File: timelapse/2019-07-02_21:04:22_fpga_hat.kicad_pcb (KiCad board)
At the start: 4 copper layers, 65 x 56.5 mm, 90 parts, among them J1 2x20, J2 AudioJack3, J3 Conn_02x06_Top_Bottom, J4 Conn_02x06_Top_Bottom, J5 Conn_02x06_Top_Bottom, J6 Conn_01x02, SW1 PTS815, SW2 PTS815, SW3 PTS815, SW4 PTS815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

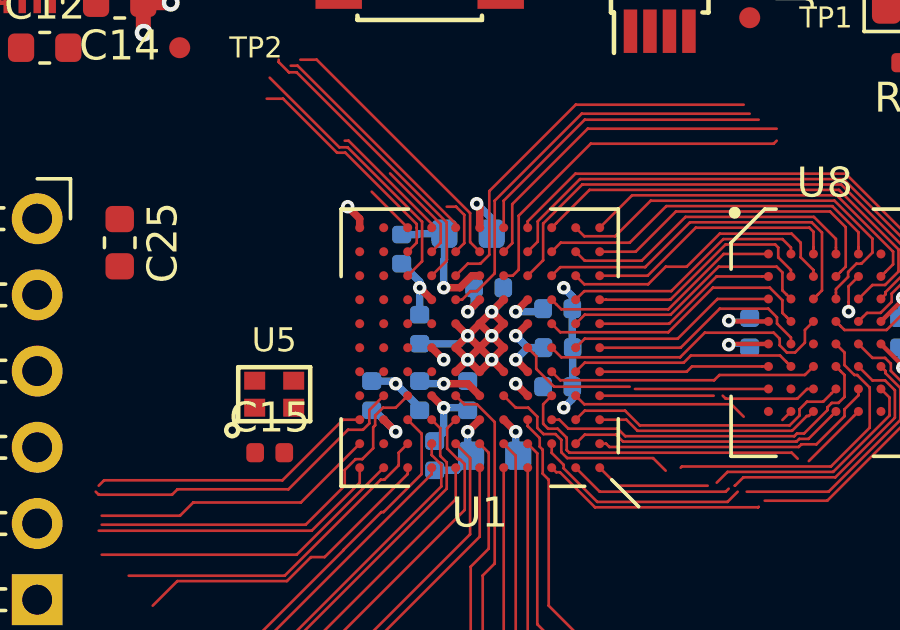
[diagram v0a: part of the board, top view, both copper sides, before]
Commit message: More FPGA escape
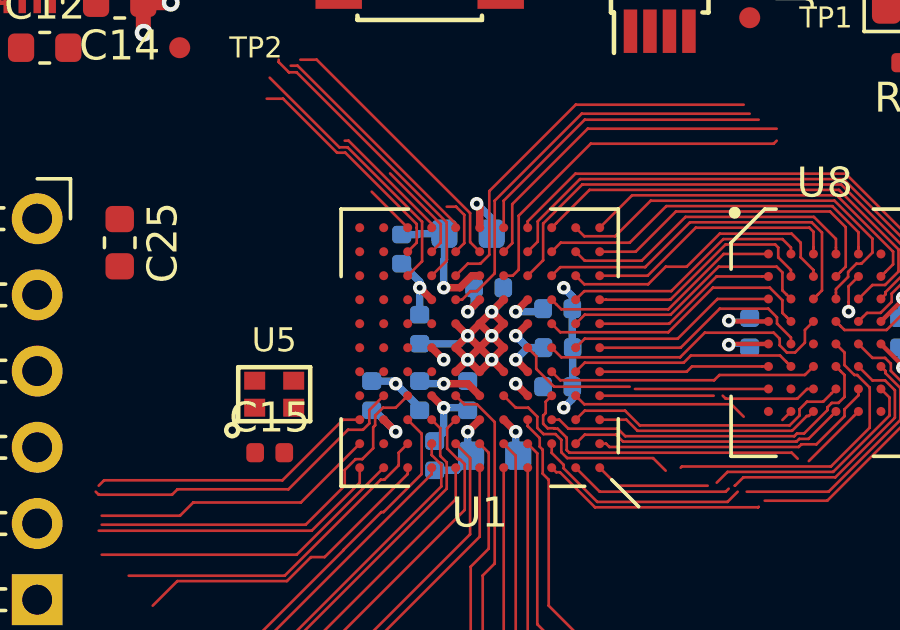
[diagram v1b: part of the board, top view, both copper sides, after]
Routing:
- net +3V3: track 13.9 -> 13.1 mm, vias 9 -> 8
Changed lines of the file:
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@@
     (thickness 1.6)
     (drawings 20)
-    (tracks 657)
+    (tracks 658)
     (zones 0)
     (modules 90)
@@
   )
   (setup
-    (last_trace_width 0.25)
+    (last_trace_width 0.09)
     (user_trace_width 0.15)
     (user_trace_width 0.25)
     (user_trace_width 0.5)
     (trace_clearance 0.09)
-    (zone_clearance 0.1)
+    (zone_clearance 0.2)
     (zone_45_only yes)
     (trace_min 0.09)
@@
   (segment (start 134.100004 106.5) (end 133.7 106.900004) (width 0.25) (layer B.Cu) (net 7))
   (segment (start 134.63 106.5) (end 134.100004 106.5) (width 0.25) (layer B.Cu) (net 7))
-  (via (at 128.1 101.8) (size 0.45) (drill 0.2) (layers F.Cu B.Cu) (net 7))
-  (segment (start 128.5 102.5) (end 128.5 102.2) (width 0.25) (layer F.Cu) (net 7))
-  (segment (start 128.5 102.2) (end 128.1 101.8) (width 0.25) (layer F.Cu) (net 7))
   (segment (start 116.5 95) (end 116.75 95) (width 0.15) (layer F.Cu) (net 9))
   (segment (start 115.5 94.485) (end 115.985 94.485) (width 0.15) (layer F.Cu) (net 9))
@@
   (segment (start 135.489099 110) (end 142.9 110) (width 0.09) (layer F.Cu) (net 118))
   (segment (start 135.4 109.910901) (end 135.489099 110) (width 0.09) (layer F.Cu) (net 118))
-  (segment (start 134.614999 108.385001) (end 134.614999 109.036801) (width 0.09) (layer F.Cu) (net 118))
+  (segment (start 135.4 109.5) (end 135.4 109.910901) (width 0.09) (layer F.Cu) (net 118))
   (segment (start 135.100002 109.200002) (end 135.4 109.5) (width 0.09) (layer F.Cu) (net 118))
-  (segment (start 134.9 108.1) (end 134.614999 108.385001) (width 0.09) (layer F.Cu) (net 118))
-  (segment (start 134.614999 109.036801) (end 134.778199 109.200001) (width 0.09) (layer F.Cu) (net 118))
-  (segment (start 134.778199 109.200001) (end 135.100002 109.200002) (width 0.09) (layer F.Cu) (net 118))
+  (segment (start 135.000001 109.200001) (end 135.100002 109.200002) (width 0.09) (layer F.Cu) (net 118))
+  (segment (start 134.985001 109.185001) (end 135.000001 109.200001) (width 0.09) (layer F.Cu) (net 118))
+  (segment (start 134.9 108.1) (end 134.7 108.3) (width 0.09) (layer F.Cu) (net 118))
+  (segment (start 134.7 108.3) (end 134.7 108.678198) (width 0.09) (layer F.Cu) (net 118))
+  (segment (start 134.614999 109.036801) (end 134.763199 109.185001) (width 0.09) (layer F.Cu) (net 118))
+  (segment (start 134.7 108.678198) (end 134.614999 108.763199) (width 0.09) (layer F.Cu) (net 118))
+  (segment (start 134.614999 108.763199) (end 134.614999 109.036801) (width 0.09) (layer F.Cu) (net 118))
   (segment (start 142.9 110) (end 143.1 110.2) (width 0.09) (layer F.Cu) (net 118))
-  (segment (start 135.4 109.5) (end 135.4 109.910901) (width 0.09) (layer F.Cu) (net 118))
+  (segment (start 134.763199 109.185001) (end 134.985001 109.185001) (width 0.09) (layer F.Cu) (net 118))
   (segment (start 143.490966 102.50011) (end 143.625 102.634144) (width 0.09) (layer F.Cu) (net 119))
   (segment (start 143.625 102.634144) (end 143.625 103.162868) (width 0.09) (layer F.Cu) (net 119))
@@
     (connect_pads (clearance 0.2))
     (min_thickness 0.2)
-    (fill yes (arc_segments 32) (thermal_gap 0.21) (thermal_bridge_width 0.21))
+    (fill (arc_segments 32) (thermal_gap 0.21) (thermal_bridge_width 0.21))
     (polygon
       (pts
@@
     (connect_pads (clearance 0.2))
     (min_thickness 0.2)
-    (fill yes (arc_segments 32) (thermal_gap 0.21) (thermal_bridge_width 0.21))
+    (fill (arc_segments 32) (thermal_gap 0.21) (thermal_bridge_width 0.21))
     (polygon
       (pts
@@
   )
   (zone (net 2) (net_name +1V2) (layer In2.Cu) (hatch edge 0.508)
-    (priority 2)
-    (connect_pads (clearance 0.12))
-    (min_thickness 0.12)
-    (fill yes (arc_segments 32) (thermal_gap 0.13) (thermal_bridge_width 0.13))
+    (priority 1)
+    (connect_pads (clearance 0.2))
+    (min_thickness 0.2)
+    (fill (arc_segments 32) (thermal_gap 0.21) (thermal_bridge_width 0.21))
     (polygon
       (pts
         (xy 134.6 105.1) (xy 134.1 105.6) (xy 133.6 105.6) (xy 132.9 104.9) (xy 131.9 104.9)
-        (xy 131.2 104.9) (xy 130.9 105.2) (xy 130.9 105.5) (xy 130.9 106.1) (xy 130.9 107.7)
-        (xy 131.5 108.4) (xy 132.4 108.4) (xy 133.4 107.4) (xy 134 107.4) (xy 134.5 107.9)
-        (xy 134.5 108.7) (xy 133.6 109.6) (xy 131.4 109.6) (xy 119.9 98.1) (xy 119.9 91.8)
-        (xy 122.3 91.8) (xy 123.8 93.3) (xy 123.8 98.1) (xy 128.6 102.9) (xy 134.6 102.9)
+        (xy 131.2 104.9) (xy 130.9 105.2) (xy 130.9 105.5) (xy 130.9 106.1) (xy 130.9 107.4)
+        (xy 132.2 108.7) (xy 133.8 108.7) (xy 134.4 108.1) (xy 134.7 108.1) (xy 135.1 108.5)
+        (xy 135.1 109.2) (xy 134.7 109.6) (xy 131.6 109.6) (xy 129.7 107.7) (xy 119.9 97.9)
+        (xy 119.9 91.8) (xy 122.3 91.8) (xy 123.8 93.3) (xy 123.8 98.1) (xy 128.6 102.9)
+        (xy 134.6 102.9)
       )
     )
@@
     (connect_pads (clearance 0.2))
     (min_thickness 0.2)
-    (fill yes (arc_segments 32) (thermal_gap 0.21) (thermal_bridge_width 0.21))
+    (fill (arc_segments 32) (thermal_gap 0.21) (thermal_bridge_width 0.21))
     (polygon
       (pts
@@
       )
     )
-  )
-  (zone (net 7) (net_name +3V3) (layer In2.Cu) (hatch edge 0.508)
-    (priority 1)
-    (connect_pads (clearance 0.1))
-    (min_thickness 0.1)
-    (fill yes (arc_segments 32) (thermal_gap 0.11) (thermal_bridge_width 0.11) (smoothing chamfer))
-    (polygon
-      (pts
-        (xy 126.9 100.8) (xy 126.9 111.8) (xy 138.9 111.8) (xy 138.9 100.8)
-      )
-    )
